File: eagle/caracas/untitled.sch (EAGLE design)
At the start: 19 parts, among them IC2 4011N, Q1 IRLZ44Z, X1 22-23-2021, X2 22-23-2021, X3 22-23-2041, X4 22-23-2041, X5 22-23-2021, X6 22-23-2021

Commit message: Remove obsolete component from electronics schematics. Clean up board paths.
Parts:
- removed IC2: 4011N, 40xx:4011N
- removed R5: (no value), rcl:R-EU_0207/10
- added IC1: 4001N, 40xx:4001N
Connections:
- removed net N$16: IC2A.I1, IC2B.O
- removed net RPI_SET: IC2A.I0
- new net MOSFET_ON: IC1A.I1, IC1B.O, Q1.G
- net +5V: now also IC1P.VDD; no longer IC2P.VDD
- net GND: now also IC1P.VSS, X3-1.S; no longer IC2P.VSS, R5.2
- net N$1: now also IC1A.O, IC1B.I0; no longer IC2A.O, IC2B.I0, Q1.G
- net POWER_STATE: now also IC1A.I0; no longer R5.1
- net RPI_RESET: now also IC1B.I1; no longer IC2B.I1
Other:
- moved on the sheet: D1, Q1
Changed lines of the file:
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@@
 <part name="U$2" library="caracas" deviceset="MKDS3" device=""/>
 <part name="SUPPLY9" library="supply2" deviceset="GND" device=""/>
-<part name="SUPPLY10" library="supply2" deviceset="GND" device=""/>
-<part name="SUPPLY11" library="supply2" deviceset="GND" device=""/>
 <part name="SUPPLY2" library="supply2" deviceset="GND" device=""/>
 <part name="U$1" library="mpc3008" deviceset="MCP3008-I/P" device=""/>
 <part name="R2" library="rcl" deviceset="R-EU_" device="0207/10"/>
-<part name="R5" library="rcl" deviceset="R-EU_" device="0207/10"/>
 <part name="SUPPLY3" library="supply2" deviceset="GND" device=""/>
 <part name="R8" library="rcl" deviceset="R-EU_" device="0207/10"/>
@@
 <part name="X4" library="con-molex" deviceset="22-23-2041" device=""/>
 <part name="Q1" library="transistor-power" deviceset="IRLZ44Z" device=""/>
-<part name="IC2" library="40xx" deviceset="4011" device="N"/>
 <part name="D1" library="diode" deviceset="1N4728" device=""/>
+<part name="IC1" library="40xx" deviceset="4001" device="N"/>
 </parts>
 <sheets>
@@
 <instance part="U$2" gate="G$1" x="12.7" y="-60.96" rot="R270"/>
 <instance part="SUPPLY9" gate="GND" x="25.4" y="5.08"/>
-<instance part="SUPPLY10" gate="GND" x="53.34" y="5.08"/>
-<instance part="SUPPLY11" gate="GND" x="91.44" y="5.08"/>
 <instance part="SUPPLY2" gate="GND" x="35.56" y="5.08"/>
 <instance part="U$1" gate="A" x="-25.4" y="35.56"/>
 <instance part="R2" gate="G$1" x="35.56" y="53.34" rot="R270"/>
-<instance part="R5" gate="G$1" x="35.56" y="30.48" rot="R270"/>
 <instance part="SUPPLY3" gate="GND" x="-48.26" y="2.54"/>
 <instance part="R8" gate="G$1" x="-76.2" y="-12.7" rot="R90"/>
@@
 <instance part="U$2" gate="G$3" x="-2.54" y="-60.96" rot="R270"/>
 <instance part="U$2" gate="G$4" x="2.54" y="-60.96" rot="R270"/>
-<instance part="Q1" gate="G$1" x="114.3" y="45.72"/>
-<instance part="IC2" gate="A" x="86.36" y="43.18"/>
-<instance part="IC2" gate="B" x="86.36" y="22.86"/>
-<instance part="IC2" gate="P" x="25.4" y="30.48"/>
-<instance part="D1" gate="1" x="53.34" y="30.48" rot="R90"/>
+<instance part="Q1" gate="G$1" x="114.3" y="25.4"/>
+<instance part="D1" gate="1" x="35.56" y="30.48" rot="R90"/>
+<instance part="IC1" gate="A" x="86.36" y="43.18"/>
+<instance part="IC1" gate="B" x="86.36" y="22.86"/>
+<instance part="IC1" gate="P" x="25.4" y="30.48"/>
 </instances>
 <busses>
@@
 </segment>
 <segment>
-<wire x1="53.34" y1="12.7" x2="53.34" y2="7.62" width="0.1524" layer="91"/>
-<pinref part="SUPPLY10" gate="GND" pin="GND"/>
 <pinref part="SUPPLY9" gate="GND" pin="GND"/>
 <wire x1="25.4" y1="7.62" x2="25.4" y2="12.7" width="0.1524" layer="91"/>
@@
 <junction x="25.4" y="12.7"/>
 <wire x1="25.4" y1="12.7" x2="35.56" y2="12.7" width="0.1524" layer="91"/>
-<wire x1="35.56" y1="25.4" x2="35.56" y2="12.7" width="0.1524" layer="91"/>
 <pinref part="SUPPLY2" gate="GND" pin="GND"/>
 <junction x="35.56" y="12.7"/>
 <wire x1="35.56" y1="12.7" x2="35.56" y2="7.62" width="0.1524" layer="91"/>
-<pinref part="R5" gate="G$1" pin="2"/>
-<wire x1="35.56" y1="12.7" x2="53.34" y2="12.7" width="0.1524" layer="91"/>
-<wire x1="53.34" y1="12.7" x2="91.44" y2="12.7" width="0.1524" layer="91"/>
-<wire x1="91.44" y1="12.7" x2="116.84" y2="12.7" width="0.1524" layer="91"/>
-<wire x1="116.84" y1="12.7" x2="116.84" y2="40.64" width="0.1524" layer="91"/>
+<wire x1="35.56" y1="12.7" x2="116.84" y2="12.7" width="0.1524" layer="91"/>
+<wire x1="116.84" y1="12.7" x2="116.84" y2="20.32" width="0.1524" layer="91"/>
 <pinref part="Q1" gate="G$1" pin="S"/>
-<pinref part="IC2" gate="P" pin="VSS"/>
-<junction x="53.34" y="12.7"/>
-<pinref part="SUPPLY11" gate="GND" pin="GND"/>
-<wire x1="91.44" y1="12.7" x2="91.44" y2="7.62" width="0.1524" layer="91"/>
-<junction x="91.44" y="12.7"/>
+<pinref part="IC1" gate="P" pin="VSS"/>
 <pinref part="D1" gate="1" pin="A"/>
-<wire x1="53.34" y1="27.94" x2="53.34" y2="12.7" width="0.1524" layer="91"/>
+<wire x1="35.56" y1="27.94" x2="35.56" y2="12.7" width="0.1524" layer="91"/>
 </segment>
 <segment>
@@
 <pinref part="SUPPLY3" gate="GND" pin="GND"/>
 <wire x1="-53.34" y1="10.16" x2="-48.26" y2="10.16" width="0.1524" layer="91"/>
-<wire x1="-53.34" y1="10.16" x2="-53.34" y2="-30.48" width="0.1524" layer="91"/>
+<wire x1="-53.34" y1="10.16" x2="-53.34" y2="-35.56" width="0.1524" layer="91"/>
+<pinref part="X3" gate="-1" pin="S"/>
 </segment>
 <segment>
@@
 <segment>
 <wire x1="35.56" y1="48.26" x2="35.56" y2="45.72" width="0.1524" layer="91"/>
-<wire x1="35.56" y1="45.72" x2="35.56" y2="35.56" width="0.1524" layer="91"/>
-<wire x1="35.56" y1="45.72" x2="53.34" y2="45.72" width="0.1524" layer="91"/>
+<pinref part="R2" gate="G$1" pin="2"/>
+<label x="55.88" y="60.96" size="1.778" layer="95"/>
+<pinref part="IC1" gate="A" pin="I0"/>
+<wire x1="78.74" y1="45.72" x2="53.34" y2="45.72" width="0.1524" layer="91"/>
+<wire x1="53.34" y1="45.72" x2="35.56" y2="45.72" width="0.1524" layer="91"/>
+<junction x="53.34" y="45.72"/>
+<wire x1="53.34" y1="45.72" x2="53.34" y2="63.5" width="0.1524" layer="91"/>
+<pinref part="D1" gate="1" pin="C"/>
+<wire x1="35.56" y1="33.02" x2="35.56" y2="45.72" width="0.1524" layer="91"/>
 <junction x="35.56" y="45.72"/>
-<pinref part="R2" gate="G$1" pin="2"/>
-<pinref part="R5" gate="G$1" pin="1"/>
-<wire x1="53.34" y1="45.72" x2="63.5" y2="45.72" width="0.1524" layer="91"/>
-<wire x1="53.34" y1="45.72" x2="53.34" y2="63.5" width="0.1524" layer="91"/>
-<junction x="53.34" y="45.72"/>
-<label x="55.88" y="60.96" size="1.778" layer="95"/>
-<pinref part="D1" gate="1" pin="C"/>
-<wire x1="53.34" y1="45.72" x2="53.34" y2="33.02" width="0.1524" layer="91"/>
 </segment>
 </net>
@@
 <wire x1="25.4" y1="63.5" x2="25.4" y2="38.1" width="0.1524" layer="91"/>
 <label x="25.4" y="66.04" size="1.778" layer="95"/>
-<pinref part="IC2" gate="P" pin="VDD"/>
+<pinref part="IC1" gate="P" pin="VDD"/>
 </segment>
 <segment>
@@
 <net name="N$1" class="0">
 <segment>
-<wire x1="99.06" y1="43.18" x2="111.76" y2="43.18" width="0.1524" layer="91"/>
-<pinref part="Q1" gate="G$1" pin="G"/>
-<pinref part="IC2" gate="A" pin="O"/>
 <wire x1="93.98" y1="43.18" x2="99.06" y2="43.18" width="0.1524" layer="91"/>
 <wire x1="99.06" y1="43.18" x2="99.06" y2="35.56" width="0.1524" layer="91"/>
@@
 <wire x1="76.2" y1="35.56" x2="71.12" y2="30.48" width="0.1524" layer="91"/>
 <wire x1="71.12" y1="30.48" x2="71.12" y2="25.4" width="0.1524" layer="91"/>
-<pinref part="IC2" gate="B" pin="I0"/>
+<pinref part="IC1" gate="A" pin="O"/>
+<pinref part="IC1" gate="B" pin="I0"/>
 <wire x1="71.12" y1="25.4" x2="78.74" y2="25.4" width="0.1524" layer="91"/>
-<junction x="99.06" y="43.18"/>
 </segment>
 </net>
 <net name="+5V_SW_GND" class="1">
 <segment>
-<wire x1="116.84" y1="50.8" x2="116.84" y2="55.88" width="0.1524" layer="91"/>
+<wire x1="116.84" y1="30.48" x2="116.84" y2="55.88" width="0.1524" layer="91"/>
 <wire x1="116.84" y1="55.88" x2="129.54" y2="55.88" width="0.1524" layer="91"/>
 <label x="116.84" y="55.88" size="1.778" layer="95"/>
@@
 </segment>
 </net>
-<net name="N$16" class="0">
-<segment>
-<pinref part="IC2" gate="B" pin="O"/>
+<net name="MOSFET_ON" class="0">
+<segment>
 <wire x1="93.98" y1="22.86" x2="99.06" y2="22.86" width="0.1524" layer="91"/>
 <wire x1="99.06" y1="22.86" x2="99.06" y2="30.48" width="0.1524" layer="91"/>
@@
 <wire x1="76.2" y1="30.48" x2="71.12" y2="35.56" width="0.1524" layer="91"/>
 <wire x1="71.12" y1="35.56" x2="71.12" y2="40.64" width="0.1524" layer="91"/>
-<pinref part="IC2" gate="A" pin="I1"/>
+<pinref part="IC1" gate="B" pin="O"/>
+<label x="99.06" y="20.32" size="1.778" layer="95"/>
+<pinref part="Q1" gate="G$1" pin="G"/>
+<wire x1="99.06" y1="22.86" x2="111.76" y2="22.86" width="0.1524" layer="91"/>
+<junction x="99.06" y="22.86"/>
+<pinref part="IC1" gate="A" pin="I1"/>
 <wire x1="71.12" y1="40.64" x2="78.74" y2="40.64" width="0.1524" layer="91"/>
-</segment>
-</net>
-<net name="RPI_SET" class="0">
-<segment>
-<pinref part="IC2" gate="A" pin="I0"/>
-<wire x1="78.74" y1="45.72" x2="63.5" y2="45.72" width="0.1524" layer="91"/>
 </segment>
 </net>
@@
 <wire x1="-60.96" y1="33.02" x2="-60.96" y2="-2.54" width="0.1524" layer="91"/>
 <wire x1="-60.96" y1="-2.54" x2="63.5" y2="-2.54" width="0.1524" layer="91"/>
-<pinref part="IC2" gate="B" pin="I1"/>
-<wire x1="78.74" y1="20.32" x2="63.5" y2="20.32" width="0.1524" layer="91"/>
 <wire x1="63.5" y1="-2.54" x2="63.5" y2="20.32" width="0.1524" layer="91"/>
-</segment>
-</net>
+<pinref part="IC1" gate="B" pin="I1"/>
+<wire x1="63.5" y1="20.32" x2="78.74" y2="20.32" width="0.1524" layer="91"/>
+</segment>
+</net>

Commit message: Update schematics again.
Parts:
- added R1, R3: (no value), rcl:R-EU_0207/10
- added T1: (no value), transistor:MPS2222A-NPN-TO92-CBE
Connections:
- new net N$2: IC1B.I1, R1.2, T1.C
- new net N$9: R3.1, T1.B
- net +12V_IGN: now also IC1A.I0
- net +5V: no longer IC1P.VDD
- net GND: now also T1.E
- net MOSFET_ON: no longer Q1.G
- net N$1: now also Q1.G
- net POWER_STATE: no longer IC1A.I0
- net RPI_RESET: now also R3.2; no longer IC1B.I1
- net VCC: now also IC1P.VDD, R1.1
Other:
- moved on the sheet: D1, IC1A, IC1B, IC1P, Q1, R13, R14, R15, R2, R8, R9, U$1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

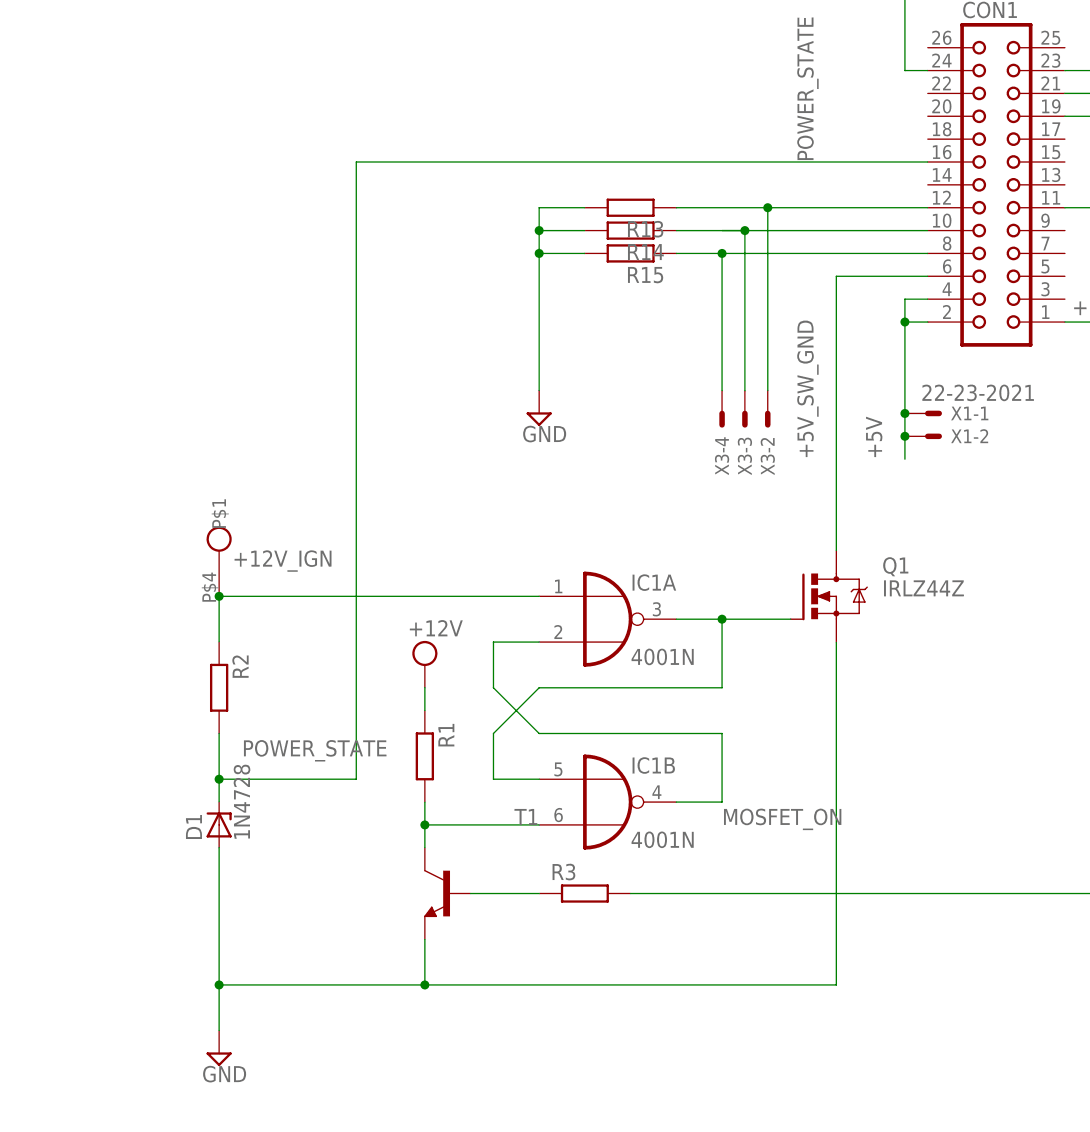
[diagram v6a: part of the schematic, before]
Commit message: Assign values to resistors.
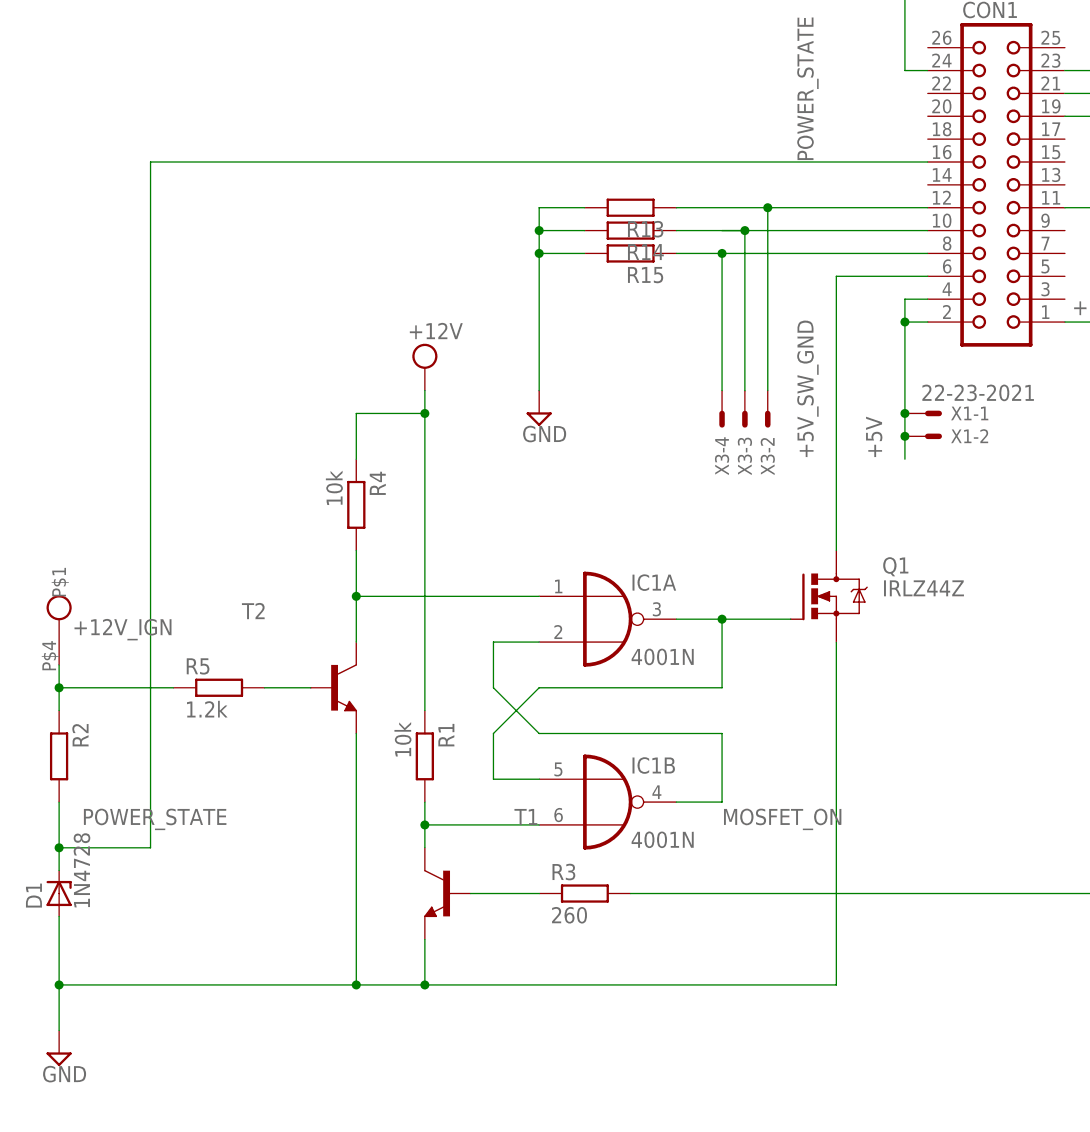
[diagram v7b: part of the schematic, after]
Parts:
- added R4: 10k, rcl:R-EU_0207/10
- added R5: 1.2k, rcl:R-EU_0207/10
- added T2: (no value), transistor:BC547-NPN-TO92-CBE
- R1: value (none) -> 10k
- R3: value (none) -> 260
- T1: device transistor:MPS2222A-NPN-TO92-CBE -> transistor:BC547-NPN-TO92-CBE
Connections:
- new net N$11: IC1A.I0, R4.2, T2.C
- new net N$12: R5.2, T2.B
- net +12V_IGN: now also R5.1; no longer IC1A.I0
- net GND: now also T2.E
- net VCC: now also R4.1
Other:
- moved on the sheet: D1, R2
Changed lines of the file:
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@@
 <part name="SUPPLY1" library="supply2" deviceset="GND" device=""/>
 <part name="+12V1" library="supply2" deviceset="VCC" device="" value="+12V"/>
-<part name="R1" library="rcl" deviceset="R-EU_" device="0207/10"/>
-<part name="T1" library="transistor" deviceset="*-NPN-" device="TO92-CBE" technology="MPS2222A"/>
-<part name="R3" library="rcl" deviceset="R-EU_" device="0207/10"/>
+<part name="R1" library="rcl" deviceset="R-EU_" device="0207/10" value="10k"/>
+<part name="T1" library="transistor" deviceset="*-NPN-" device="TO92-CBE" technology="BC547"/>
+<part name="R3" library="rcl" deviceset="R-EU_" device="0207/10" value="260"/>
+<part name="R4" library="rcl" deviceset="R-EU_" device="0207/10" value="10k"/>
+<part name="T2" library="transistor" deviceset="*-NPN-" device="TO92-CBE" technology="BC547"/>
+<part name="R5" library="rcl" deviceset="R-EU_" device="0207/10" value="1.2k"/>
 </parts>
 <sheets>
@@
 <instance part="CON1" gate="A" x="-78.74" y="35.56"/>
 <instance part="U$2" gate="G$1" x="-40.64" y="-53.34" rot="R270"/>
-<instance part="SUPPLY2" gate="GND" x="-165.1" y="-60.96"/>
+<instance part="SUPPLY2" gate="GND" x="-182.88" y="-60.96"/>
 <instance part="U$1" gate="A" x="0" y="35.56"/>
-<instance part="R2" gate="G$1" x="-165.1" y="-20.32" rot="R270"/>
+<instance part="R2" gate="G$1" x="-182.88" y="-27.94" rot="R270"/>
 <instance part="SUPPLY3" gate="GND" x="-22.86" y="5.08"/>
 <instance part="R8" gate="G$1" x="-38.1" y="35.56" rot="R180"/>
@@
 <instance part="X4" gate="-2" x="-27.94" y="55.88" rot="R90"/>
 <instance part="U$2" gate="G$3" x="-40.64" y="-12.7" rot="R90"/>
-<instance part="U$2" gate="G$4" x="-165.1" y="-5.08" rot="R90"/>
+<instance part="U$2" gate="G$4" x="-182.88" y="-12.7" rot="R90"/>
 <instance part="Q1" gate="G$1" x="-99.06" y="-10.16"/>
-<instance part="D1" gate="1" x="-165.1" y="-35.56" rot="R90"/>
+<instance part="D1" gate="1" x="-182.88" y="-43.18" rot="R90"/>
 <instance part="IC1" gate="A" x="-121.92" y="-12.7"/>
 <instance part="IC1" gate="B" x="-121.92" y="-33.02"/>
@@
 <instance part="+12V2" gate="G$1" x="-48.26" y="-15.24"/>
 <instance part="SUPPLY1" gate="GND" x="-48.26" y="-50.8"/>
-<instance part="+12V1" gate="G$1" x="-142.24" y="-17.78"/>
+<instance part="+12V1" gate="G$1" x="-142.24" y="15.24"/>
 <instance part="R1" gate="G$1" x="-142.24" y="-27.94" rot="R270"/>
 <instance part="T1" gate="G$1" x="-139.7" y="-43.18" rot="MR0"/>
 <instance part="R3" gate="G$1" x="-124.46" y="-43.18"/>
+<instance part="R4" gate="G$1" x="-149.86" y="0" rot="R270"/>
+<instance part="T2" gate="G$1" x="-152.4" y="-20.32"/>
+<instance part="R5" gate="G$1" x="-165.1" y="-20.32"/>
 </instances>
 <busses>
@@
 <pinref part="SUPPLY2" gate="GND" pin="GND"/>
 <pinref part="D1" gate="1" pin="A"/>
-<wire x1="-165.1" y1="-38.1" x2="-165.1" y2="-53.34" width="0.1524" layer="91"/>
+<wire x1="-182.88" y1="-45.72" x2="-182.88" y2="-53.34" width="0.1524" layer="91"/>
 <pinref part="T1" gate="G$1" pin="E"/>
-<wire x1="-165.1" y1="-53.34" x2="-165.1" y2="-58.42" width="0.1524" layer="91"/>
-<wire x1="-165.1" y1="-53.34" x2="-142.24" y2="-53.34" width="0.1524" layer="91"/>
+<wire x1="-182.88" y1="-53.34" x2="-182.88" y2="-58.42" width="0.1524" layer="91"/>
+<wire x1="-182.88" y1="-53.34" x2="-149.86" y2="-53.34" width="0.1524" layer="91"/>
+<wire x1="-149.86" y1="-53.34" x2="-142.24" y2="-53.34" width="0.1524" layer="91"/>
 <wire x1="-142.24" y1="-53.34" x2="-142.24" y2="-48.26" width="0.1524" layer="91"/>
-<junction x="-165.1" y="-53.34"/>
+<junction x="-182.88" y="-53.34"/>
 <pinref part="Q1" gate="G$1" pin="S"/>
 <wire x1="-96.52" y1="-15.24" x2="-96.52" y2="-53.34" width="0.1524" layer="91"/>
 <wire x1="-96.52" y1="-53.34" x2="-142.24" y2="-53.34" width="0.1524" layer="91"/>
 <junction x="-142.24" y="-53.34"/>
+<pinref part="T2" gate="G$1" pin="E"/>
+<wire x1="-149.86" y1="-25.4" x2="-149.86" y2="-53.34" width="0.1524" layer="91"/>
+<junction x="-149.86" y="-53.34"/>
 </segment>
 <segment>
@@
 <label x="-99.06" y="38.1" size="1.778" layer="95" rot="R90"/>
 <pinref part="CON1" gate="A" pin="16"/>
-<wire x1="-86.36" y1="38.1" x2="-149.86" y2="38.1" width="0.1524" layer="91"/>
-<wire x1="-149.86" y1="38.1" x2="-149.86" y2="-30.48" width="0.1524" layer="91"/>
-<wire x1="-165.1" y1="-25.4" x2="-165.1" y2="-30.48" width="0.1524" layer="91"/>
+<wire x1="-86.36" y1="38.1" x2="-172.72" y2="38.1" width="0.1524" layer="91"/>
+<wire x1="-172.72" y1="38.1" x2="-172.72" y2="-38.1" width="0.1524" layer="91"/>
+<wire x1="-182.88" y1="-33.02" x2="-182.88" y2="-38.1" width="0.1524" layer="91"/>
 <pinref part="R2" gate="G$1" pin="2"/>
-<label x="-162.56" y="-27.94" size="1.778" layer="95"/>
+<label x="-180.34" y="-35.56" size="1.778" layer="95"/>
 <pinref part="D1" gate="1" pin="C"/>
-<wire x1="-165.1" y1="-30.48" x2="-165.1" y2="-33.02" width="0.1524" layer="91"/>
-<wire x1="-165.1" y1="-30.48" x2="-149.86" y2="-30.48" width="0.1524" layer="91"/>
-<junction x="-165.1" y="-30.48"/>
+<wire x1="-182.88" y1="-38.1" x2="-182.88" y2="-40.64" width="0.1524" layer="91"/>
+<wire x1="-182.88" y1="-38.1" x2="-172.72" y2="-38.1" width="0.1524" layer="91"/>
+<junction x="-182.88" y="-38.1"/>
 </segment>
 </net>
 <net name="+12V_IGN" class="2">
 <segment>
-<wire x1="-165.1" y1="-15.24" x2="-165.1" y2="-10.16" width="0.1524" layer="91"/>
 <label x="17.78" y="45.72" size="1.778" layer="95"/>
 <pinref part="R2" gate="G$1" pin="1"/>
-<pinref part="IC1" gate="A" pin="I0"/>
-<wire x1="-165.1" y1="-10.16" x2="-129.54" y2="-10.16" width="0.1524" layer="91"/>
 <pinref part="U$2" gate="G$4" pin="P$1"/>
-<junction x="-165.1" y="-10.16"/>
-<label x="-152.4" y="-5.08" size="1.778" layer="95" rot="R180"/>
+<label x="-170.18" y="-12.7" size="1.778" layer="95" rot="R180"/>
+<wire x1="-182.88" y1="-22.86" x2="-182.88" y2="-20.32" width="0.1524" layer="91"/>
+<pinref part="R5" gate="G$1" pin="1"/>
+<wire x1="-182.88" y1="-20.32" x2="-182.88" y2="-17.78" width="0.1524" layer="91"/>
+<wire x1="-182.88" y1="-20.32" x2="-170.18" y2="-20.32" width="0.1524" layer="91"/>
+<junction x="-182.88" y="-20.32"/>
 </segment>
 </net>
@@
 <pinref part="+12V1" gate="G$1" pin="VCC"/>
 <pinref part="R1" gate="G$1" pin="1"/>
-<wire x1="-142.24" y1="-20.32" x2="-142.24" y2="-22.86" width="0.1524" layer="91"/>
+<wire x1="-142.24" y1="12.7" x2="-142.24" y2="10.16" width="0.1524" layer="91"/>
+<pinref part="R4" gate="G$1" pin="1"/>
+<wire x1="-142.24" y1="10.16" x2="-142.24" y2="-22.86" width="0.1524" layer="91"/>
+<wire x1="-149.86" y1="5.08" x2="-149.86" y2="10.16" width="0.1524" layer="91"/>
+<wire x1="-149.86" y1="10.16" x2="-142.24" y2="10.16" width="0.1524" layer="91"/>
+<junction x="-142.24" y="10.16"/>
 </segment>
 </net>
@@
 </segment>
 </net>
+<net name="N$11" class="0">
+<segment>
+<pinref part="IC1" gate="A" pin="I0"/>
+<wire x1="-129.54" y1="-10.16" x2="-149.86" y2="-10.16" width="0.1524" layer="91"/>
+<pinref part="R4" gate="G$1" pin="2"/>
+<wire x1="-149.86" y1="-10.16" x2="-149.86" y2="-5.08" width="0.1524" layer="91"/>
+<pinref part="T2" gate="G$1" pin="C"/>
+<wire x1="-149.86" y1="-10.16" x2="-149.86" y2="-15.24" width="0.1524" layer="91"/>
+<junction x="-149.86" y="-10.16"/>
+</segment>
+</net>
+<net name="N$12" class="0">
+<segment>
+<pinref part="R5" gate="G$1" pin="2"/>
+<pinref part="T2" gate="G$1" pin="B"/>
+<wire x1="-160.02" y1="-20.32" x2="-154.94" y2="-20.32" width="0.1524" layer="91"/>
+</segment>
+</net>
